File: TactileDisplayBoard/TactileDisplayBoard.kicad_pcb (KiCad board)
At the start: 2 copper layers, 97 x 70 mm, 12 parts, among them J1 Conn_01x02, J2 Conn_01x02, J3 Microstep_Jumper, J4 Conn_Motor, J5 Microstep_Jumper, J6 Conn_Motor, J7 PowerSwitch, U1 A4988, U2 ESP32-DEVKITC, U3 A4988

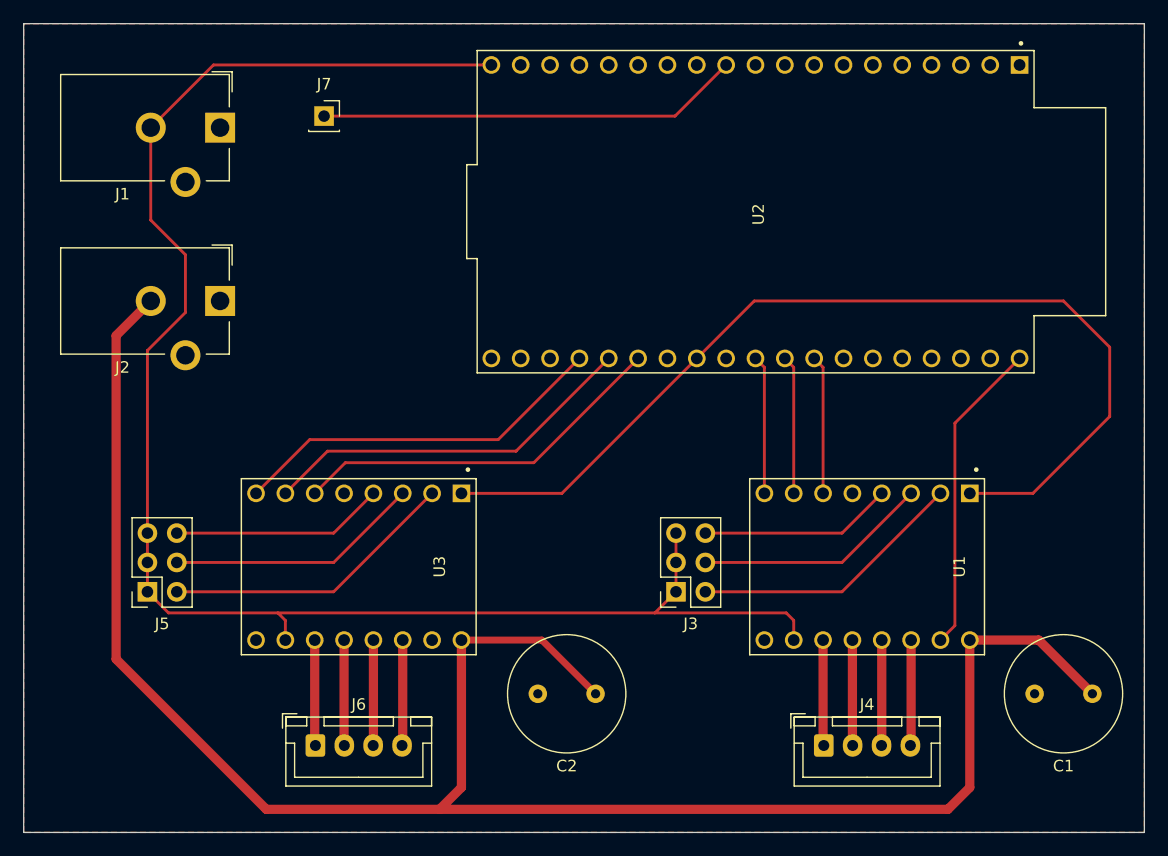
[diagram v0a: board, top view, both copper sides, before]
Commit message: Added BLE, and wrote firmware for ESP32 in Display Driver
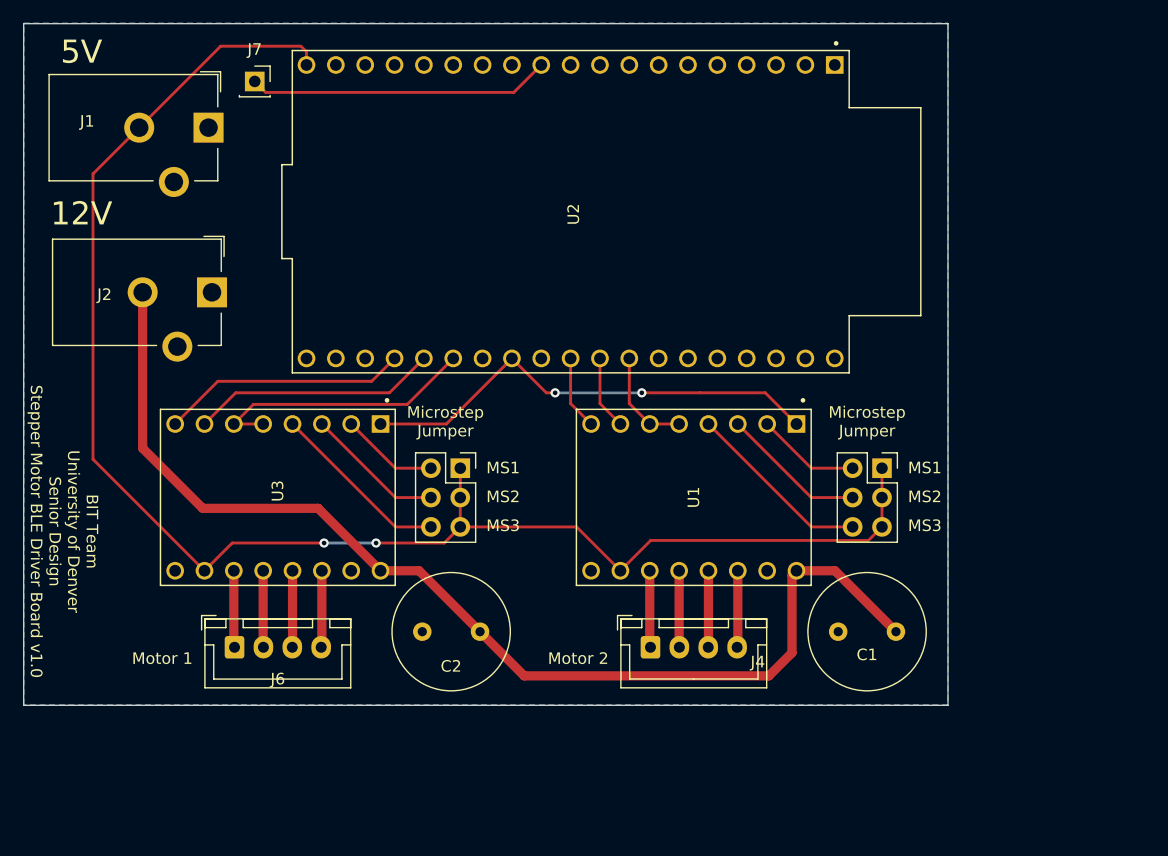
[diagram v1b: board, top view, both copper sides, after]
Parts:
- moved J5 29.1 mm to (124.8, 76.5), turned to 0 degrees
- moved J3 20.8 mm to (161.3, 76.5), turned to 0 degrees
- moved C1 17.8 mm to (162.5, 90.6)
- moved J4 17.2 mm to (141.2, 92.0)
- moved U1 16.2 mm to (145.0, 79.0)
- moved U2 16.0 mm to (134.3, 54.3)
- moved C2 11.4 mm to (126.5, 90.6)
- moved J6 11.0 mm to (105.2, 92.0)
- moved U3 9.22 mm to (109.0, 79.0)
- moved J7 6.71 mm to (107.0, 43.0)
- moved J2 1.03 mm to (103.3, 61.2)
- moved J1 1.00 mm to (103.0, 47.0)
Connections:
- U1 pad 5: unconnected-(U1-Pad5) -> M2_SLEEP
- U3 pad 5: unconnected-(U3-Pad5) -> M1_SLEEP
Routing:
- net +12V: track 166.6 -> 96.7 mm
- net EN: track 85.5 -> 40.7 mm, vias 0 -> 2
- net GND: track 27.2 -> 0.00 mm
- net Net-(J5-Pad2): track 25.6 -> 8.48 mm
- net Net-(J3-Pad2): track 23.9 -> 8.98 mm
- net M1_STEP: track 32.8 -> 21.3 mm
- net M1_DIR: track 32.8 -> 21.3 mm
- net PS_en: track 36.6 -> 26.2 mm
- net Net-(J5-Pad4): track 22.0 -> 12.1 mm
- net M1_SLEEP: track 32.8 -> 23.9 mm
- net Net-(J3-Pad4): track 20.3 -> 12.6 mm
- net +5V: track 143.5 -> 136.3 mm, vias 0 -> 2
- net M2_STEP: track 12.0 -> 6.41 mm
- net M2_DIR: track 12.0 -> 6.41 mm
- net M2_SLEEP: track 12.0 -> 8.95 mm
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- added copper zone on B.Cu, net GND
- removed copper zone on F.Cu, net GND
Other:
- board size 97 x 70 mm -> 80 x 59 mm
- board text added: "12V"
- board text added: "5V"
- board text added: "BIT Team University of Denver Senior Design Stepper Motor BLE Driver Board v1.0"
- board text added: "JLCJLCJLCJLC"
- board text added: "MS1"
- board text added: "MS2"
- board text added: "MS3"
- board text added: "Microstep Jumper"
- board text added: "Motor 1"
- board text added: "Motor 2"
- board text added: "To Microstep: Use jumper according to A4988 datasheet"
- board text added: "Todo: Flip the direction of the esp add resistors for connections to esp flip the vd and gnd for power jack connectos"
